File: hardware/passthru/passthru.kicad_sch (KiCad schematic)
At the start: 79 parts, among them J1 ARM_SWD, J2 RJ45_LED_Shielded, J3 Screw_Terminal_01x02, Q1 Q_PMOS_DGS, Q2 Q_PMOS_DGS, Q3 Q_NPN_BEC, U1 EFM32GG11B8xx, U2 KSZ8081RND, U3 LM5085, U4 TPS2375-1

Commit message: passthru: use shielded RJ45 jack
Splurging for the shielded connector. It'll give a little extra
strength in case the cable gets yanked.
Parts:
- J2: footprint common:RJHSE-308X -> common:RJHSE-338X
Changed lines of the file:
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@@
       (effects (font (size 1.27 1.27)) hide)
     )
-    (property "Footprint" "common:RJHSE-308X" (id 2) (at 191.77 13.97 0)
+    (property "Footprint" "common:RJHSE-338X" (id 2) (at 191.77 13.97 0)
       (effects (font (size 1.27 1.27)) hide)
     )
@@
     )
     (path "/6c8aa87e-5d26-482e-85f5-61333e7cd602"
-      (reference "J2") (unit 1) (value "RJ45_LED_Shielded") (footprint "common:RJHSE-308X")
+      (reference "J2") (unit 1) (value "RJ45_LED_Shielded") (footprint "common:RJHSE-338X")
     )
     (path "/23e451cf-9eb8-44b4-a66f-a7165d67d967"

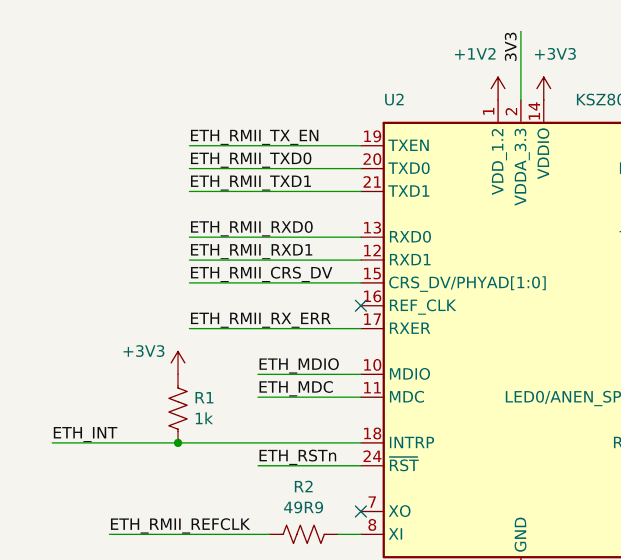
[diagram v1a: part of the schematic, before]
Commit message: passthru: add current-limit between MAC and PHY
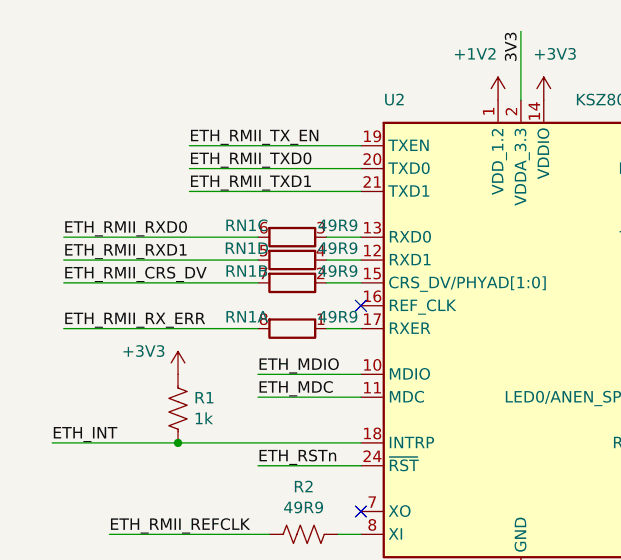
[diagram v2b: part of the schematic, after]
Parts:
- added RN1: 49R9, Resistor_SMD:R_Cat16-4, symbol Device:R_Pack04_Split
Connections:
- net ETH_RMII_CRS_DV: now also RN1.7 (R2.2); no longer U2.15 (CRS_DV/PHYAD[1:0])
- net ETH_RMII_RXD0: now also RN1.6 (R3.2); no longer U2.13 (RXD0)
- net ETH_RMII_RXD1: now also RN1.5 (R4.2); no longer U2.12 (RXD1)
- net ETH_RMII_RX_ERR: now also RN1.8 (R1.2); no longer U2.17 (RXER)
- new net: RN1.4 (R4.1), U2.12 (RXD1)
- new net: RN1.3 (R3.1), U2.13 (RXD0)
- new net: RN1.1 (R1.1), U2.17 (RXER)
- new net: RN1.2 (R2.1), U2.15 (CRS_DV/PHYAD[1:0])
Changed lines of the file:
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@@
     (stroke (width 0) (type default) (color 0 0 0 0))
   )
+  (wire (pts (xy 48.26 43.18) (xy 52.07 43.18))
+    (stroke (width 0) (type default) (color 0 0 0 0))
+  )
   (wire (pts (xy 135.89 73.66) (xy 135.89 71.12))
     (stroke (width 0) (type default) (color 0 0 0 0))
@@
     (stroke (width 0) (type default) (color 0 0 0 0))
   )
+  (wire (pts (xy 48.26 38.1) (xy 52.07 38.1))
+    (stroke (width 0) (type default) (color 0 0 0 0))
+  )
   (wire (pts (xy 212.09 20.32) (xy 227.33 20.32))
     (stroke (width 0) (type default) (color 0 0 0 0))
@@
     (stroke (width 0) (type default) (color 0 0 0 0))
   )
+  (wire (pts (xy 48.26 48.26) (xy 52.07 48.26))
+    (stroke (width 0) (type default) (color 0 0 0 0))
+  )
   (wire (pts (xy 219.71 149.86) (xy 219.71 154.94))
     (stroke (width 0) (type default) (color 0 0 0 0))
   )
-  (wire (pts (xy 33.02 40.64) (xy 52.07 40.64))
+  (wire (pts (xy 19.05 40.64) (xy 40.64 40.64))
     (stroke (width 0) (type default) (color 0 0 0 0))
   )
@@
     (stroke (width 0) (type default) (color 0 0 0 0))
   )
+  (wire (pts (xy 48.26 40.64) (xy 52.07 40.64))
+    (stroke (width 0) (type default) (color 0 0 0 0))
+  )
   (wire (pts (xy 172.72 120.65) (xy 170.18 120.65))
     (stroke (width 0) (type default) (color 0 0 0 0))
@@
     (stroke (width 0) (type default) (color 0 0 0 0))
   )
-  (wire (pts (xy 33.02 38.1) (xy 52.07 38.1))
+  (wire (pts (xy 19.05 38.1) (xy 40.64 38.1))
     (stroke (width 0) (type default) (color 0 0 0 0))
   )
@@
     (stroke (width 0) (type default) (color 0 0 0 0))
   )
-  (wire (pts (xy 33.02 43.18) (xy 52.07 43.18))
+  (wire (pts (xy 19.05 43.18) (xy 40.64 43.18))
     (stroke (width 0) (type default) (color 0 0 0 0))
   )
@@
     (stroke (width 0) (type default) (color 0 0 0 0))
   )
-  (wire (pts (xy 33.02 48.26) (xy 52.07 48.26))
+  (wire (pts (xy 19.05 48.26) (xy 40.64 48.26))
     (stroke (width 0) (type default) (color 0 0 0 0))
   )
@@
     (effects (font (size 1.27 1.27)) (justify right bottom))
   )
-  (label "ETH_RMII_RXD1" (at 33.02 40.64 0)
+  (label "ETH_RMII_RXD1" (at 19.05 40.64 0)
     (effects (font (size 1.27 1.27)) (justify left bottom))
   )
@@
     (effects (font (size 1.27 1.27)) (justify left bottom))
   )
-  (label "ETH_RMII_CRS_DV" (at 33.02 43.18 0)
+  (label "ETH_RMII_CRS_DV" (at 19.05 43.18 0)
     (effects (font (size 1.27 1.27)) (justify left bottom))
   )
@@
     (effects (font (size 1.27 1.27)) (justify left bottom))
   )
-  (label "ETH_RMII_RX_ERR" (at 33.02 48.26 0)
+  (label "ETH_RMII_RX_ERR" (at 19.05 48.26 0)
     (effects (font (size 1.27 1.27)) (justify left bottom))
   )
-  (label "ETH_RMII_RXD0" (at 33.02 38.1 0)
+  (label "ETH_RMII_RXD0" (at 19.05 38.1 0)
     (effects (font (size 1.27 1.27)) (justify left bottom))
   )
@@
     (pin "2")
   )
+  (symbol (lib_id "Device:R_Pack04_Split") (at 44.45 40.64 90) (unit 4)
+    (in_bom yes) (on_board yes)
+    (property "Reference" "RN1" (id 0) (at 39.37 39.37 90))
+    (property "Value" "49R9" (id 1) (at 49.53 39.37 90))
+    (property "Footprint" "Resistor_SMD:R_Cat16-4" (id 2) (at 44.45 42.672 90)
+      (effects (font (size 1.27 1.27)) hide)
+    )
+    (property "Datasheet" "~" (id 3) (at 44.45 40.64 0)
+      (effects (font (size 1.27 1.27)) hide)
+    )
+    (pin "1")
+    (pin "8")
+    (pin "2")
+    (pin "7")
+    (pin "3")
+    (pin "6")
+    (pin "4")
+    (pin "5")
+  )
   (symbol (lib_id "Device:C") (at 125.73 67.31 0) (unit 1)
     (in_bom yes) (on_board yes)
@@
     (pin "2")
   )
+  (symbol (lib_id "Device:R_Pack04_Split") (at 44.45 38.1 90) (unit 3)
+    (in_bom yes) (on_board yes)
+    (property "Reference" "RN1" (id 0) (at 39.37 36.83 90))
+    (property "Value" "49R9" (id 1) (at 49.53 36.83 90))
+    (property "Footprint" "Resistor_SMD:R_Cat16-4" (id 2) (at 44.45 40.132 90)
+      (effects (font (size 1.27 1.27)) hide)
+    )
+    (property "Datasheet" "~" (id 3) (at 44.45 38.1 0)
+      (effects (font (size 1.27 1.27)) hide)
+    )
+    (pin "1")
+    (pin "8")
+    (pin "2")
+    (pin "7")
+    (pin "3")
+    (pin "6")
+    (pin "4")
+    (pin "5")
+  )
   (symbol (lib_id "power:+3V3") (at 100.33 173.99 0) (unit 1)
     (in_bom yes) (on_board yes)
@@
     (pin "1")
   )
+  (symbol (lib_id "Device:R_Pack04_Split") (at 44.45 48.26 90) (unit 1)
+    (in_bom yes) (on_board yes)
+    (property "Reference" "RN1" (id 0) (at 39.37 46.99 90))
+    (property "Value" "49R9" (id 1) (at 49.53 46.99 90))
+    (property "Footprint" "Resistor_SMD:R_Cat16-4" (id 2) (at 44.45 50.292 90)
+      (effects (font (size 1.27 1.27)) hide)
+    )
+    (property "Datasheet" "~" (id 3) (at 44.45 48.26 0)
+      (effects (font (size 1.27 1.27)) hide)
+    )
+    (pin "1")
+    (pin "8")
+    (pin "2")
+    (pin "7")
+    (pin "3")
+    (pin "6")
+    (pin "4")
+    (pin "5")
+  )
   (symbol (lib_id "power:GND") (at 181.61 165.1 0) (unit 1)
     (in_bom yes) (on_board yes)
@@
     (pin "2")
   )
+  (symbol (lib_id "Device:R_Pack04_Split") (at 44.45 43.18 90) (unit 2)
+    (in_bom yes) (on_board yes)
+    (property "Reference" "RN1" (id 0) (at 39.37 41.91 90))
+    (property "Value" "49R9" (id 1) (at 49.53 41.91 90))
+    (property "Footprint" "Resistor_SMD:R_Cat16-4" (id 2) (at 44.45 45.212 90)
+      (effects (font (size 1.27 1.27)) hide)
+    )
+    (property "Datasheet" "~" (id 3) (at 44.45 43.18 0)
+      (effects (font (size 1.27 1.27)) hide)
+    )
+    (pin "1")
+    (pin "8")
+    (pin "2")
+    (pin "7")
+    (pin "3")
+    (pin "6")
+    (pin "4")
+    (pin "5")
+  )
   (symbol (lib_id "Device:C") (at 194.31 55.88 0) (unit 1)
     (in_bom yes) (on_board yes)
@@
       (reference "R23") (unit 1) (value "10k") (footprint "Resistor_SMD:R_0603_1608Metric_Pad0.98x0.95mm_HandSolder")
     )
+    (path "/e358a910-2228-46a1-9c1a-bd70ac4676c5"
+      (reference "RN1") (unit 1) (value "49R9") (footprint "Resistor_SMD:R_Cat16-4")
+    )
+    (path "/f24c9214-754b-42cf-94b1-98e3823cffed"
+      (reference "RN1") (unit 2) (value "49R9") (footprint "Resistor_SMD:R_Cat16-4")
+    )
+    (path "/e1d09bfe-e5d6-4852-bd2b-e960572f1cbe"
+      (reference "RN1") (unit 3) (value "49R9") (footprint "Resistor_SMD:R_Cat16-4")
+    )
+    (path "/c2dfbc45-12a0-4667-81e8-5f72a7f17d3f"
+      (reference "RN1") (unit 4) (value "49R9") (footprint "Resistor_SMD:R_Cat16-4")
+    )
     (path "/c6a058cb-c0ea-45c3-8288-e93e9b637aae"

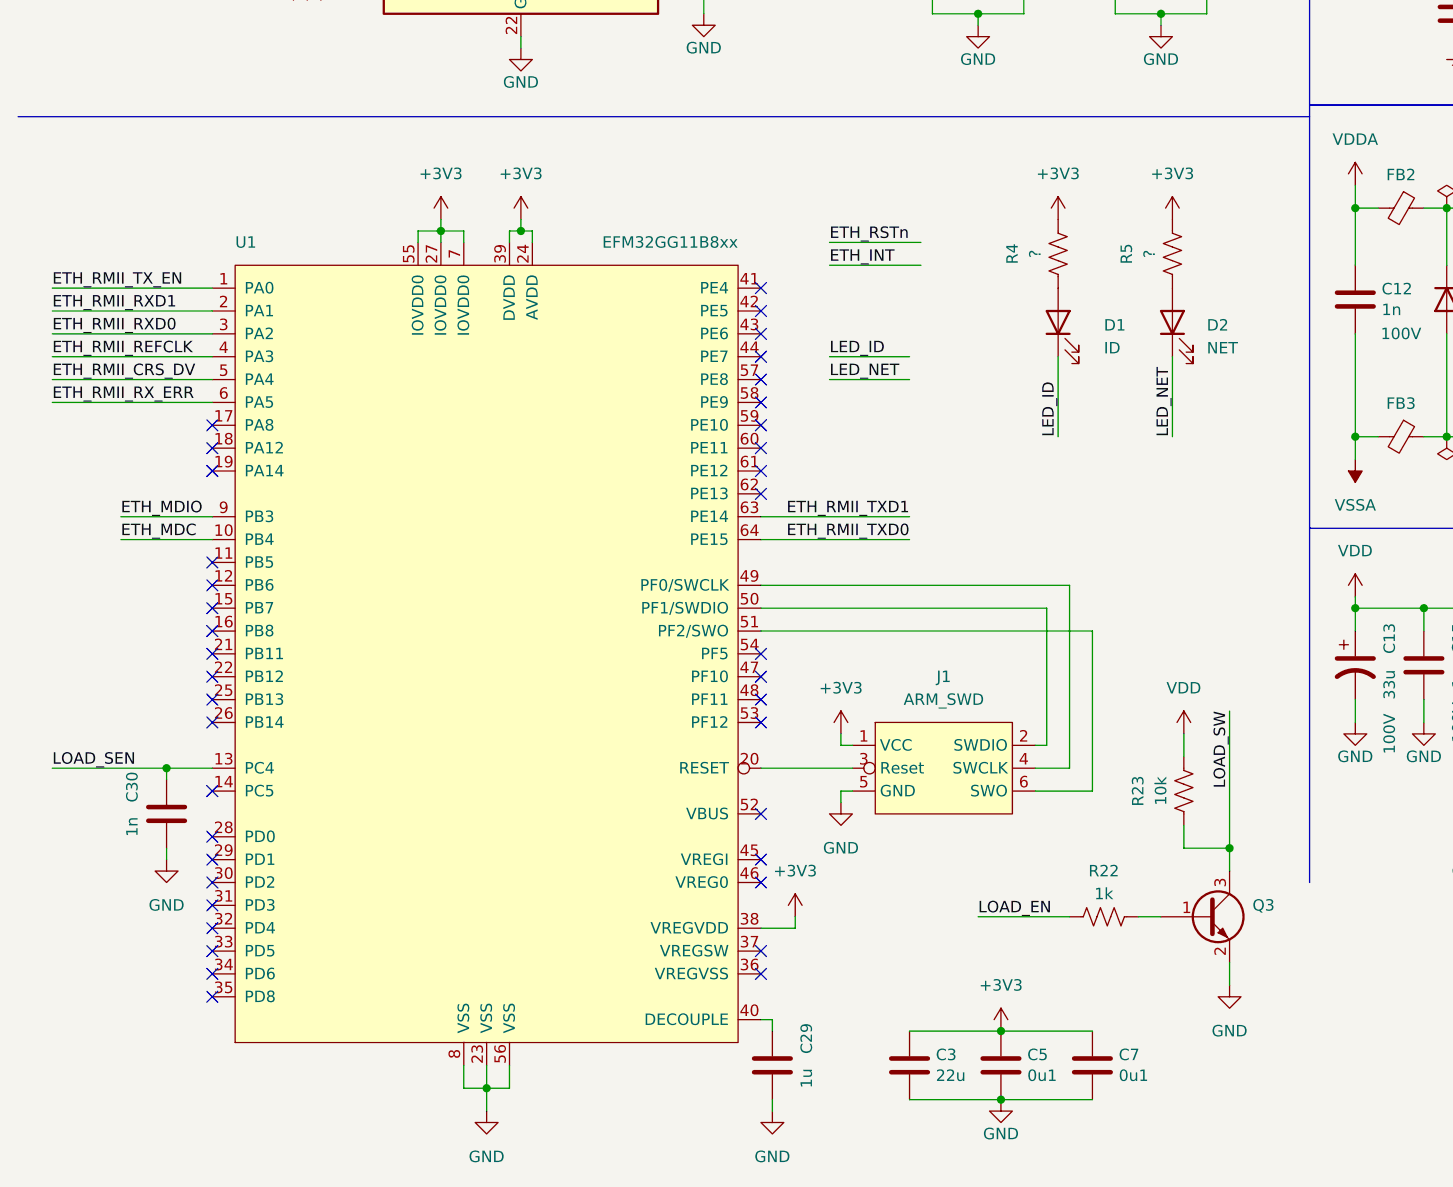
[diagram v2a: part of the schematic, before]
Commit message: passthru: add 50 MHz crystal
Not sure how I forgot this...
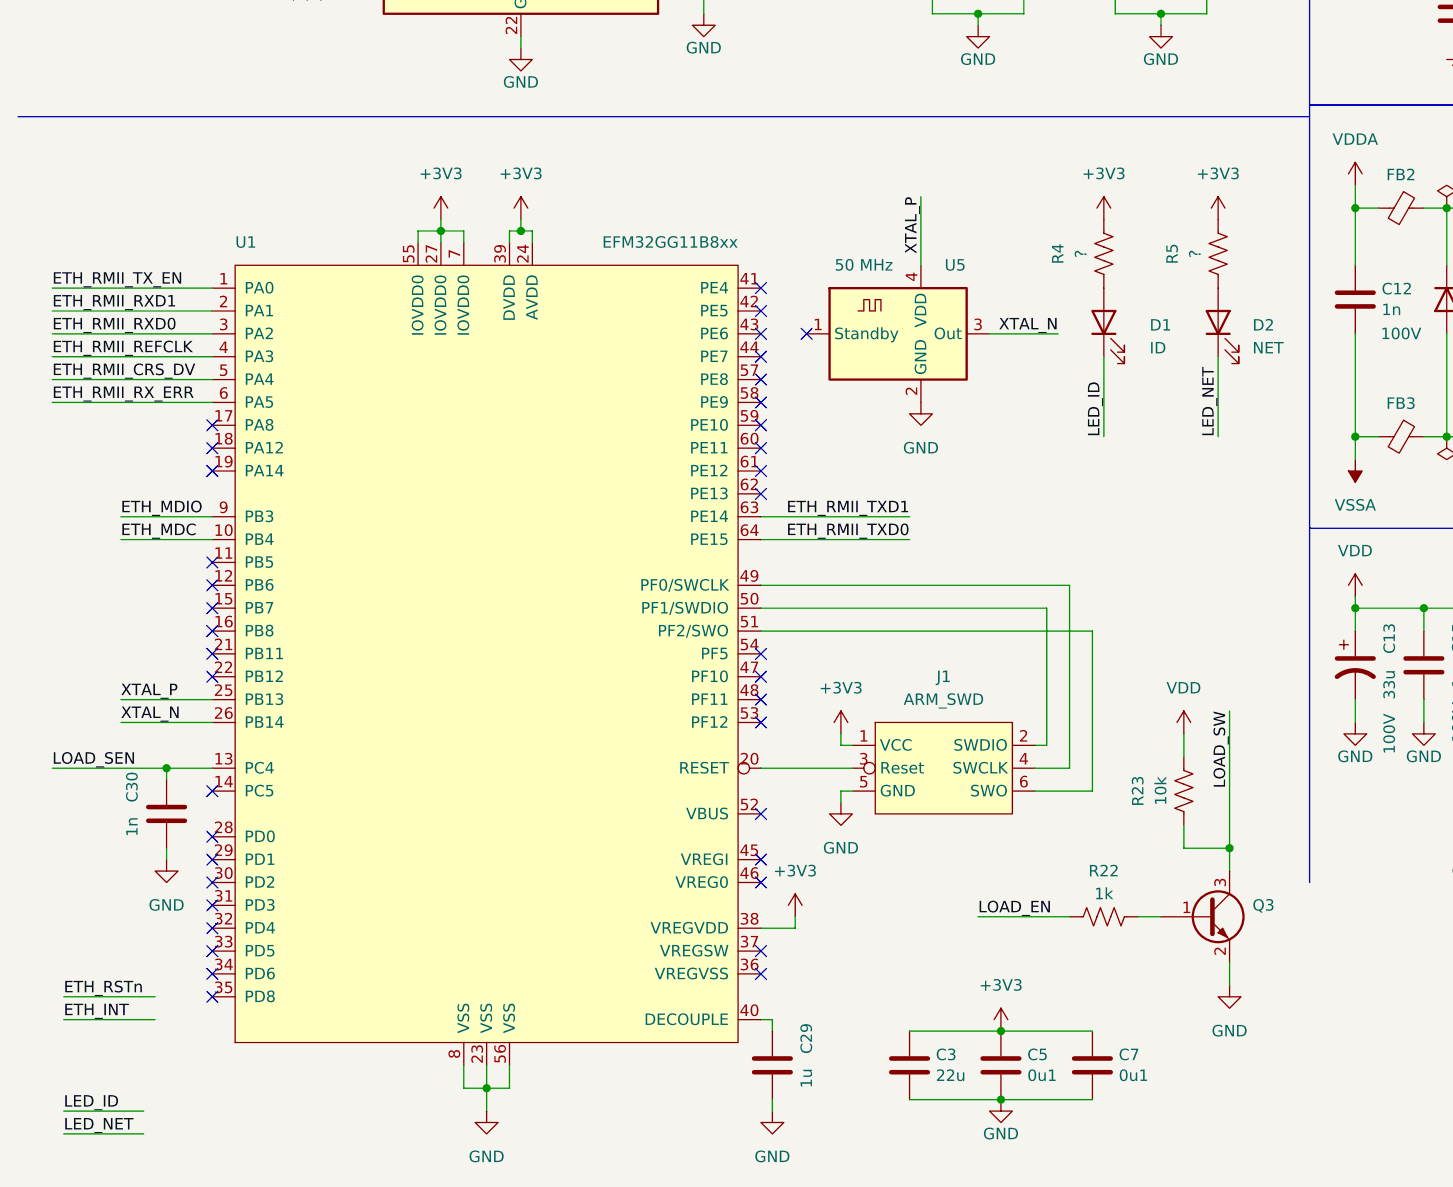
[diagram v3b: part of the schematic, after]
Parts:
- added U5: 50 MHz, Oscillator:Oscillator_SMD_SeikoEpson_SG210-4Pin_2.5x2.0mm_HandSoldering, symbol Oscillator:ASDMB-xxxMHz
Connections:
- net GND: now also U5.2 (GND)
- net XTAL_P: now reaches U1.25 (PB13)
- net XTAL_P: now also U5.4 (VDD)
- net XTAL_N: now reaches U1.26 (PB14)
- net XTAL_N: now also U5.3 (Out)
- no-connect marks 41 -> 40
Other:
- moved on the sheet: D1, D2, R4, R5

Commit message: passthru: connect Ethernet interrupt
I know enough of the layout to know that this will work well connected
anywhere between PE8 and PE13.
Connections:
- net ETH_INT: now also U1.62 (PE13)
- no-connect marks 40 -> 39
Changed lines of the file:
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@@
   (no_connect (at 96.52 180.34))
   (no_connect (at 35.56 142.24))
-  (no_connect (at 96.52 127))
   (no_connect (at 35.56 124.46))
   (no_connect (at 35.56 139.7))
@@
     (stroke (width 0) (type default) (color 0 0 0 0))
   )
-  (wire (pts (xy 29.21 185.42) (xy 19.05 185.42))
+  (wire (pts (xy 96.52 127) (xy 113.03 127))
     (stroke (width 0) (type default) (color 0 0 0 0))
   )
@@
     (effects (font (size 1.27 1.27)) (justify left bottom))
   )
-  (label "ETH_INT" (at 19.05 185.42 0)
-    (effects (font (size 1.27 1.27)) (justify left bottom))
+  (label "ETH_INT" (at 113.03 127 180)
+    (effects (font (size 1.27 1.27)) (justify right bottom))
   )
   (label "ETH_TX-" (at 259.08 35.56 180)

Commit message: passthru: route the PHY reset
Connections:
- net ETH_RSTn: now also U1.60 (PE11)
- no-connect marks 39 -> 38
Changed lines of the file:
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@@
   (no_connect (at 35.56 137.16))
   (no_connect (at 35.56 119.38))
-  (no_connect (at 96.52 121.92))
   (no_connect (at 96.52 180.34))
   (no_connect (at 35.56 142.24))
@@
     (stroke (width 0) (type default) (color 0 0 0 0))
   )
+  (wire (pts (xy 96.52 121.92) (xy 107.95 121.92))
+    (stroke (width 0) (type default) (color 0 0 0 0))
+  )
   (wire (pts (xy 176.53 151.13) (xy 176.53 154.94))
     (stroke (width 0) (type default) (color 0 0 0 0))
@@
   )
   (wire (pts (xy 97.79 185.42) (xy 97.79 186.69))
-    (stroke (width 0) (type default) (color 0 0 0 0))
-  )
-  (wire (pts (xy 19.05 182.88) (xy 29.21 182.88))
     (stroke (width 0) (type default) (color 0 0 0 0))
   )
@@
     (effects (font (size 1.27 1.27)) (justify right bottom))
   )
-  (label "ETH_RSTn" (at 19.05 182.88 0)
-    (effects (font (size 1.27 1.27)) (justify left bottom))
+  (label "ETH_RSTn" (at 107.95 121.92 180)
+    (effects (font (size 1.27 1.27)) (justify right bottom))
   )
   (label "XTAL_N" (at 129.54 109.22 180)
